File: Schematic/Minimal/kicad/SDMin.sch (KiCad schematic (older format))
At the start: 6 parts

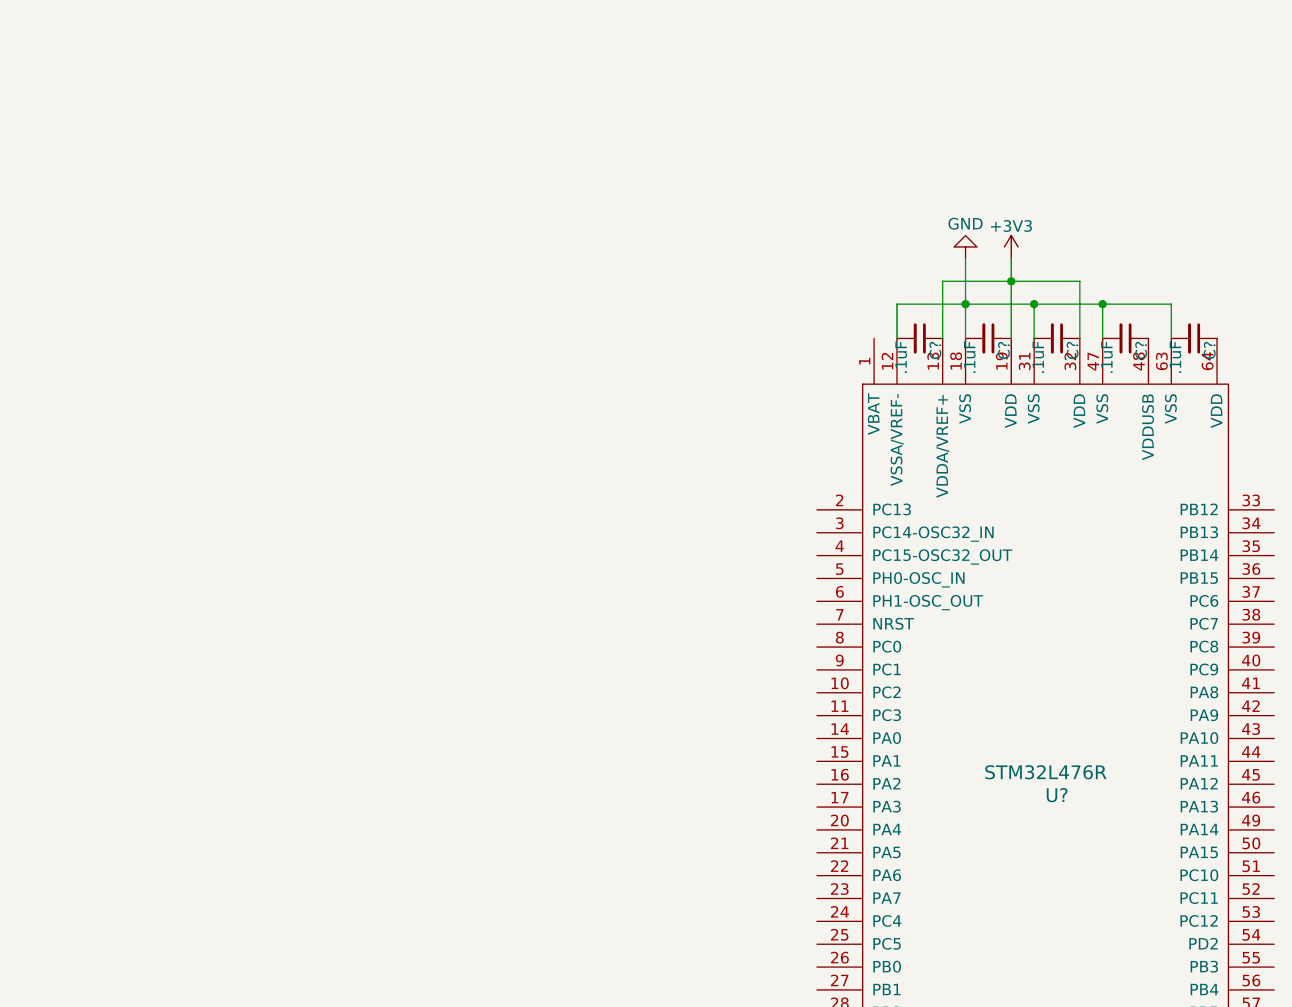
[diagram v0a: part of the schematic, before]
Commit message: Add schematic for the power subsystem, create all missing components
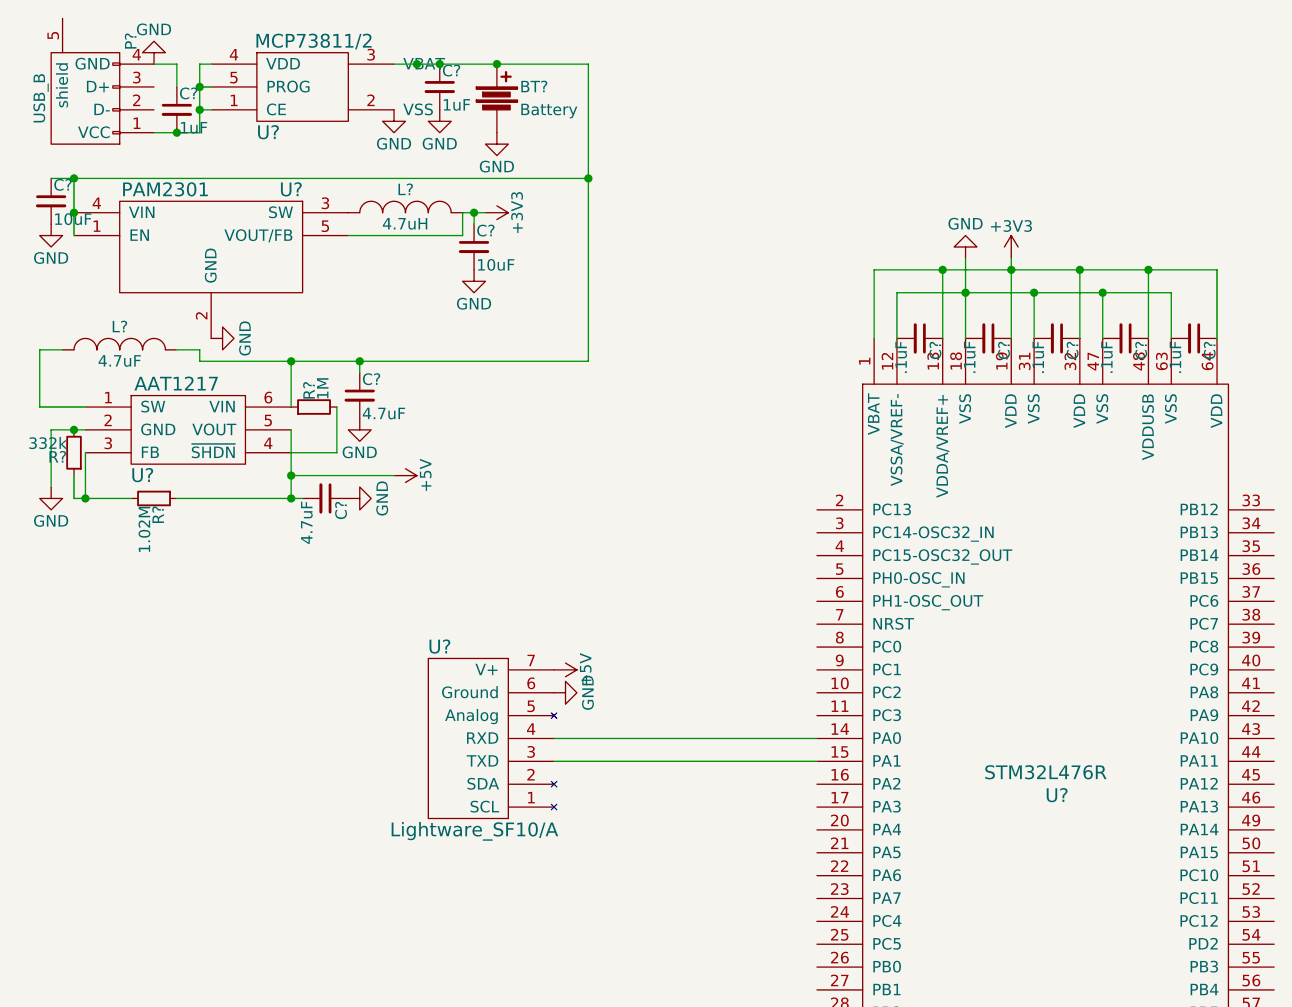
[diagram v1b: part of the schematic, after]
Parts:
- added BT?: Battery, symbol Battery
- added C? (x2): 1uF, symbol C_Small
- added C? (x2): 10uF, symbol C_Small
- added C? (x2): 4.7uF, symbol C_Small
- added L?: 4.7uH, symbol INDUCTOR_SMALL
- added L?: 4.7uF, symbol INDUCTOR_SMALL
- added P?: USB_B, symbol USB_B
- added R?: 1M, symbol R_Small
- added R?: 332k, symbol R_Small
- added R?: 1.02M, symbol R_Small
- added U?: Lightware_SF10/A, symbol Lightware_SF10/A
- added U?: MCP73811/2, symbol MCP73811/2
- added U?: PAM2301, symbol PAM2301
- added U?: AAT1217, symbol AAT1217
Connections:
- net +3V3: now also C?.1, C?.1, U?.1 (VBAT), U?.48 (VDDUSB), U?.64 (VDD), C?.1, L?.2, U?.5 (VOUT/FB)
- net GND: now also BT?.2, C?.1, C?.1, C?.2, C?.2, C?.2, C?.2, P?.4 (GND), R?.2, U?.2 (GND), U?.2 (GND), U?.6 (Ground)
- net at U?.14 (PA0): now also U?.4 (RXD)
- net at U?.15 (PA1): now also U?.3 (TXD)
- new net: BT?.1, C?.1, C?.1, C?.1, L?.2, R?.1, U?.1 (EN), U?.4 (VIN), U?.6 (VIN)
- new net: C?.2, P?.1 (VCC), U?.1 (CE), U?.4 (VDD), U?.5 (PROG)
- new net: L?.1, U?.3 (SW)
- new net: L?.1, U?.1 (SW)
- new net: R?.1, R?.2, U?.3 (FB)
- new net: R?.2, U?.4 (~SHDN)
- new net +5V: C?.2, R?.1, U?.5 (VOUT), U?.7 (V+)

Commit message: Add Codec, Bluetooth, debug to minimal schematic
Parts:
- added C? (x5): 0.1uF, symbol C_Small
- added C?: 470pF, symbol C_Small
- added C? (x2): 22pF, symbol C_Small
- added C?: 4700pF, symbol C_Small
- added CON?: SD_Card, 10067847-001, symbol SD_Card
- added R?: 1k, symbol R_Small
- added R?: 1M, symbol R_Small
- added R? (x2): 4.7, symbol R_Small
- added U?: LSM303DTR, symbol LSM303DTR
- added U?: LS20031, symbol LS20031
- added U?: STA013, symbol STA013
- added U?: RN-52, symbol RN-52
- added U?: UART, symbol UART
- added U?: ADMP401, symbol ADMP401
- added U?: DebugPins, symbol DebugPins
- added X?: 14.7456MHz, symbol CRYSTAL_SMD
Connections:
- net labels added: +BATT, GNDA, NRST, PA0_las, PA13_dbg, PA14_dbg, PA1_las, PA2_UART, PA3_UART, PA4_MP3-DR, PA5_MP3-SCK, PA6_BT-RTS, PA7_MP3-SDI, PA9_GPS-RX, PB0_BT-GP9, PB14_MP3-RST, PB1_BT-CTS, PB3_dbg, PB6_MP3-SCL, PB7_GPS-TX, PB9_MP3-SDA, PC0_mic, PC13_dbg, PC4_BT-RX, PC5_BT-TX
- wire segments 49 -> 157
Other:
- moved on the sheet: C?, U?

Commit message: Add schematic (schematic done, need to draw footprints and design PCB layout)
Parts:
- removed C? (x5): .1uF, symbol C_Small
- added C? (x6): 4.7uF, symbol C_Small
- added C?: 0.22uF, symbol C_Small
- added C?: 10uF, symbol C_Small
- added C? (x8): 100nF, symbol C_Small
- added C?: 47uF, symbol C_Small
- added R? (x5): 47K, symbol R_Small
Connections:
- net labels added: +3.3V, PA15_SD-DET, PB10_MAG-SPC, PB12_MAG-INT1, PB13_MAG-INT2, PB15_MAG-SDI, PB9_MAG-CS, PC0_MP3-SCL, PC10_SD-D2, PC11_SD-D3, PC12_SD-CK, PC1_MP3-SDA, PC2_MAG-SDO, PC3_mic, PC8_SD-D0, PC9_SD-D1, PD2_SD-CMD
- net labels removed: GNDA, PB6_MP3-SCL, PB9_MP3-SDA, PC0_mic
- wire segments 157 -> 223
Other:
- moved on the sheet: CON?, U?

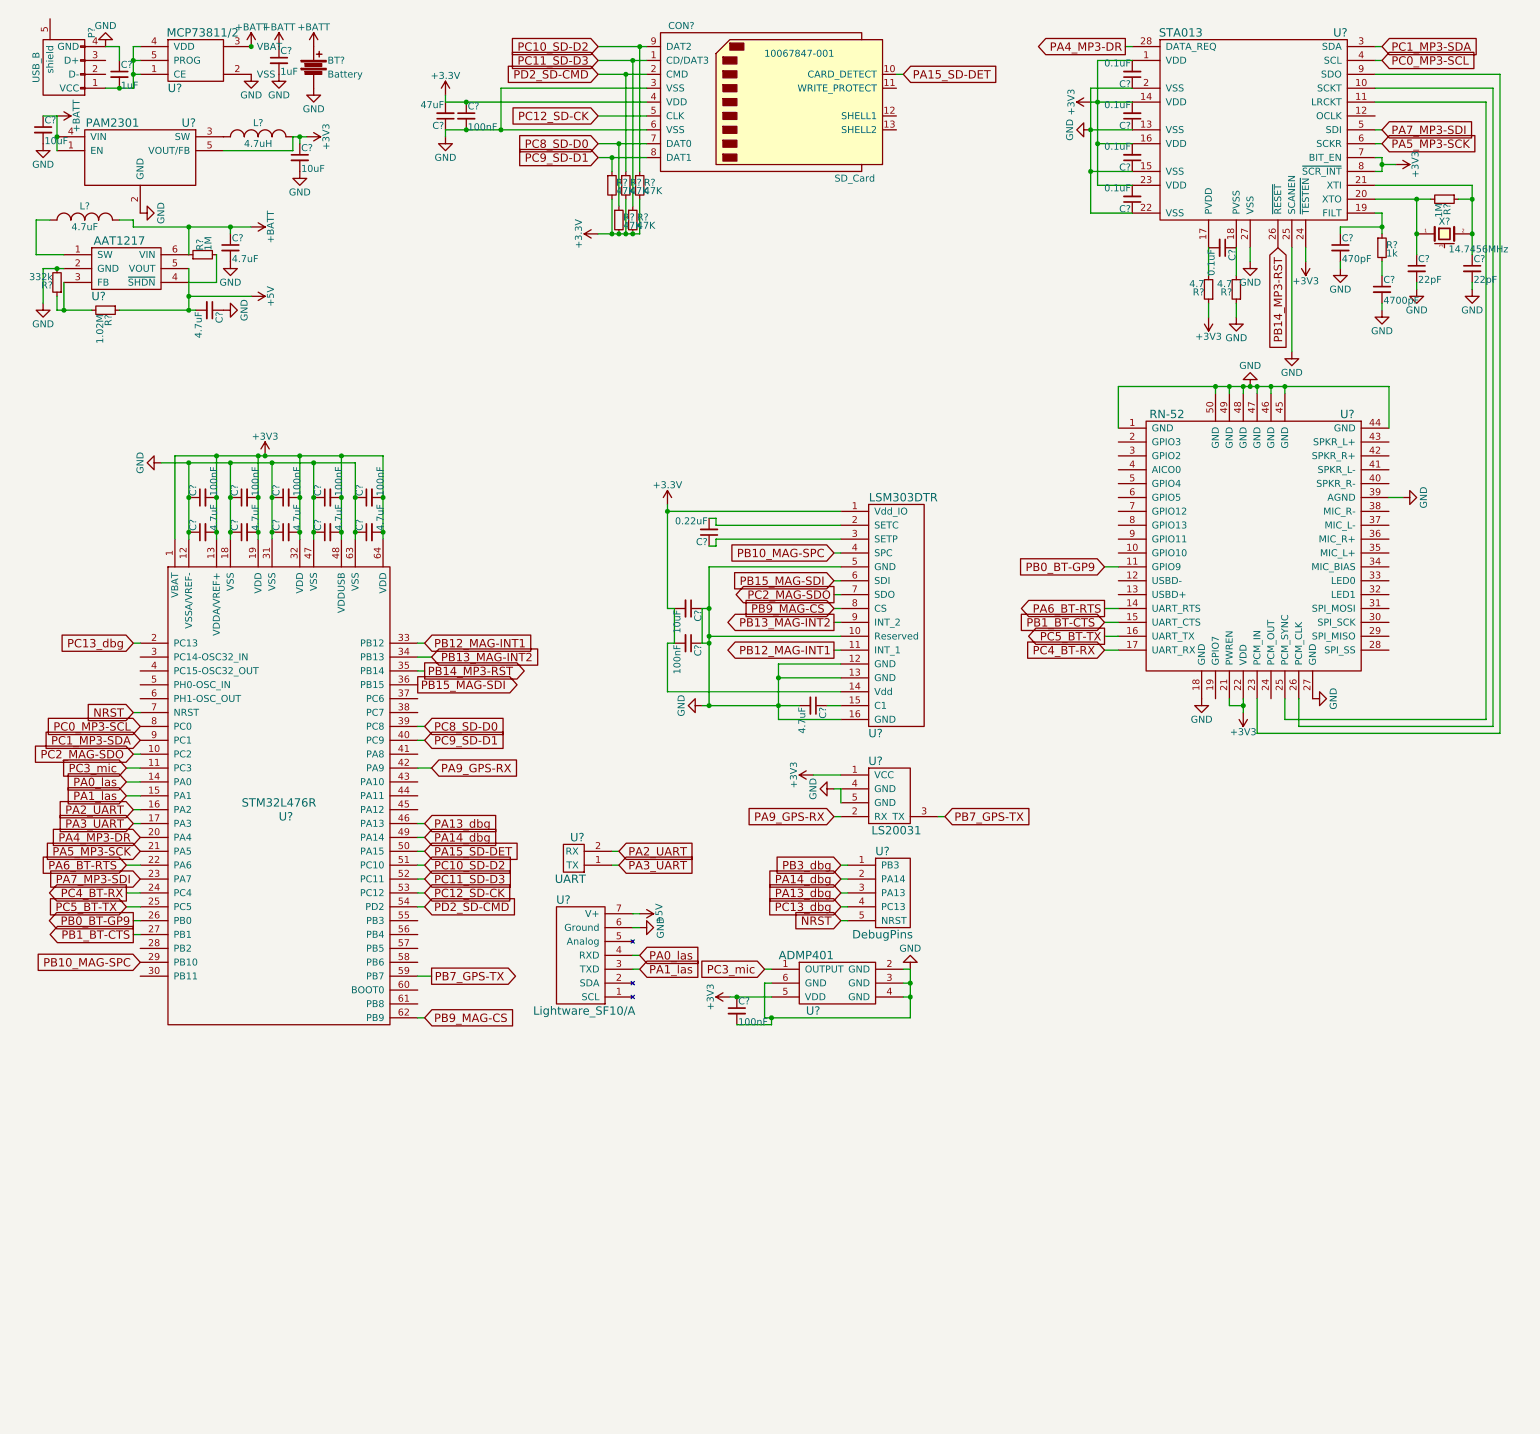
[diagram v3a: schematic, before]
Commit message: Add push buttons and battery switch to schematic
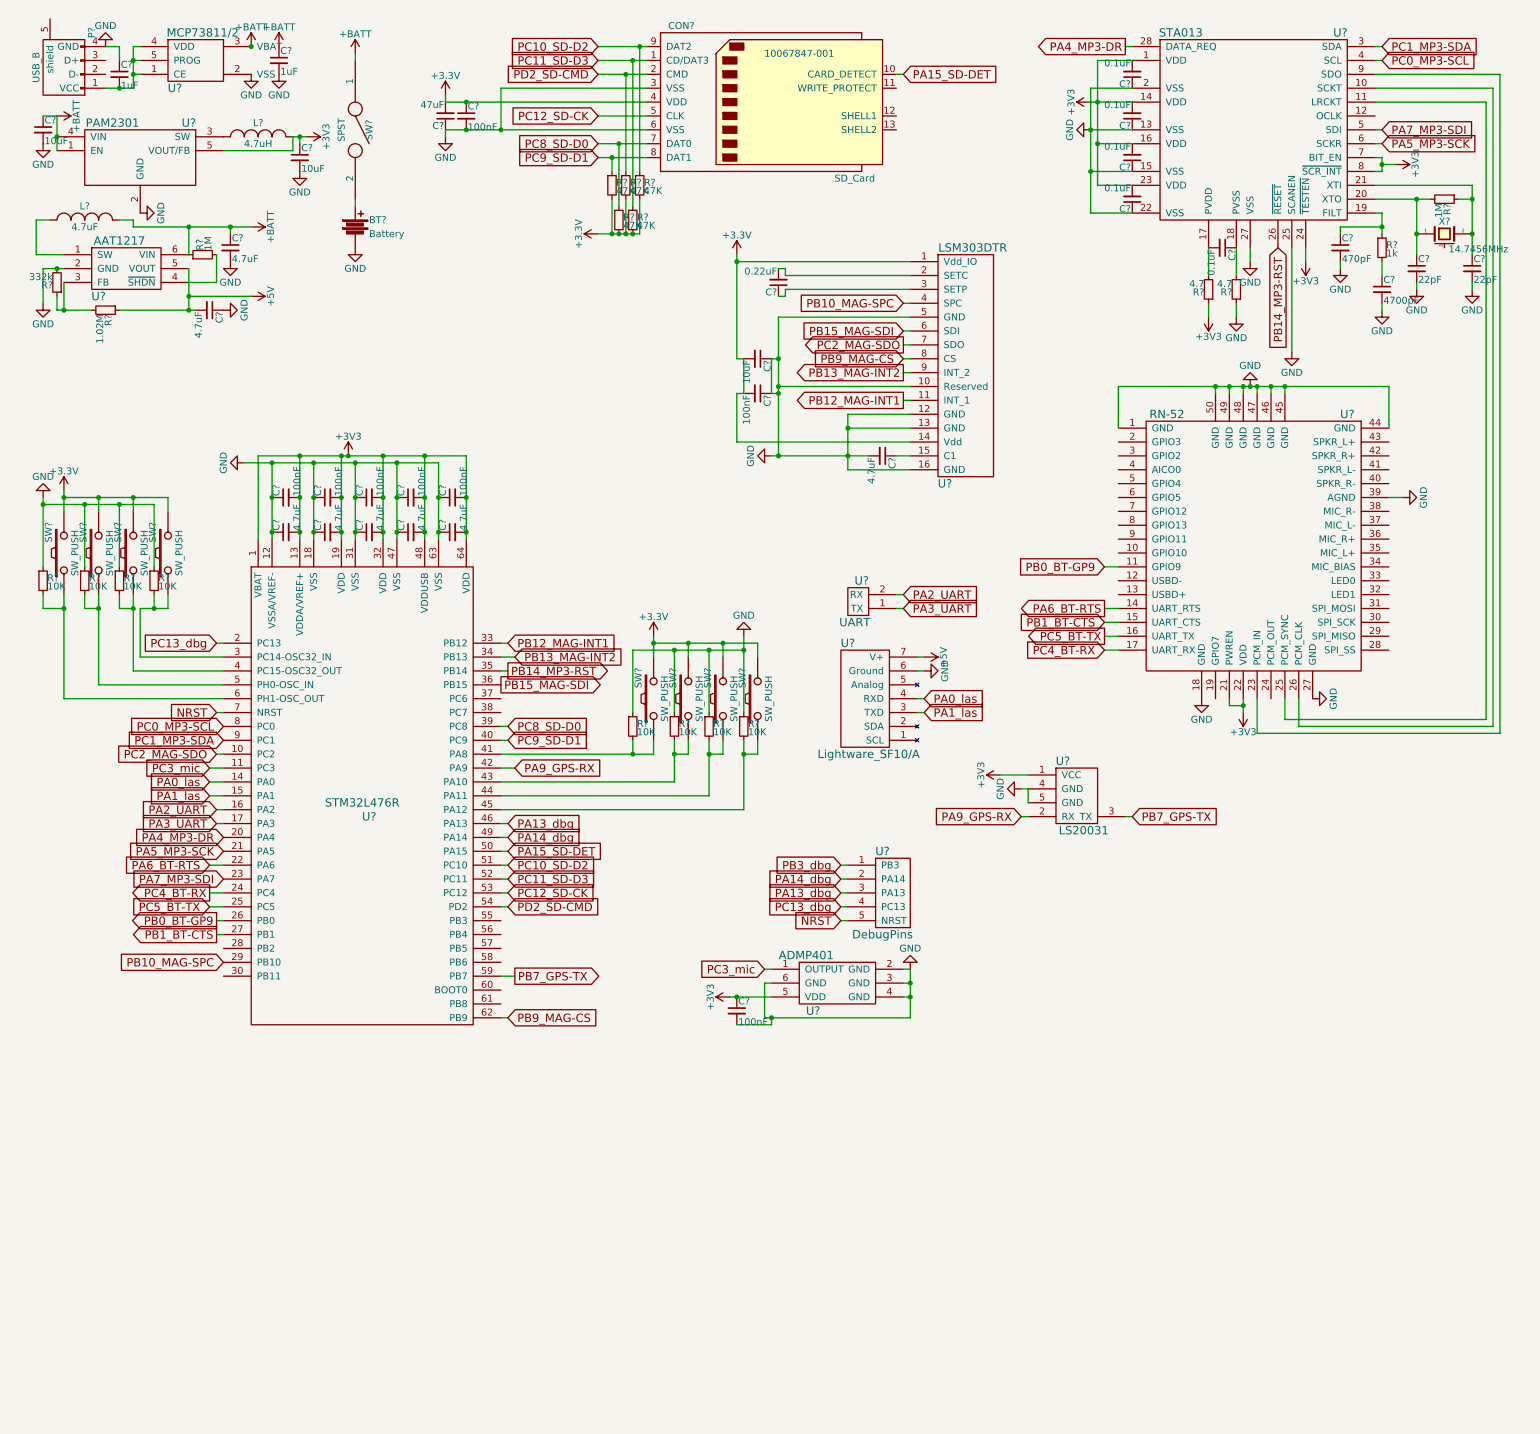
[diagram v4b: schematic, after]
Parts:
- added R? (x8): 10K, symbol R_Small
- added SW? (x8): SW_PUSH, symbol SW_PUSH
- added SW?: SPST, symbol SPST
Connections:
- net +3V3: now also SW?.2, SW?.2, SW?.2, SW?.2, SW?.2, SW?.2, SW?.2, SW?.2
- net +BATT: now also SW?.1; no longer BT?.1
- net GND: now also R?.1, R?.1, R?.1, R?.1, R?.1, R?.1, R?.1, R?.1
- net at U?.3 (PC14-OSC32_IN): now also R?.2, SW?.1
- net at U?.4 (PC15-OSC32_OUT): now also R?.2, SW?.1
- net at U?.41 (PA8): now also R?.2, SW?.1
- net at U?.43 (PA10): now also R?.2, SW?.1
- net at U?.44 (PA11): now also R?.2, SW?.1
- net at U?.45 (PA12): now also R?.2, SW?.1
- net at U?.5 (PH0-OSC_IN): now also R?.2, SW?.1
- net at U?.6 (PH1-OSC_OUT): now also R?.2, SW?.1
- new net: BT?.1, SW?.2
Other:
- moved on the sheet: BT?, C?, U?
